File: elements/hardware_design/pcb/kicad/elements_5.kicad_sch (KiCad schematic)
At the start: 42 parts

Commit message: changed led/switch
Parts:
- removed SW1: (no value), symbol elements-eagle-import:LP4OA1PBCT
- added SW1: SW_MEC_5G_2LED, Supercell 1.3:C&K_D6R, symbol Switch:SW_MEC_5G_2LED
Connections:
- net GND: now also SW1.3 (K), SW1.4 (A)
- net SW_GATE: now also SW1.1
- net at R10.2: now also SW1.2
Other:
- moved on the sheet: R10

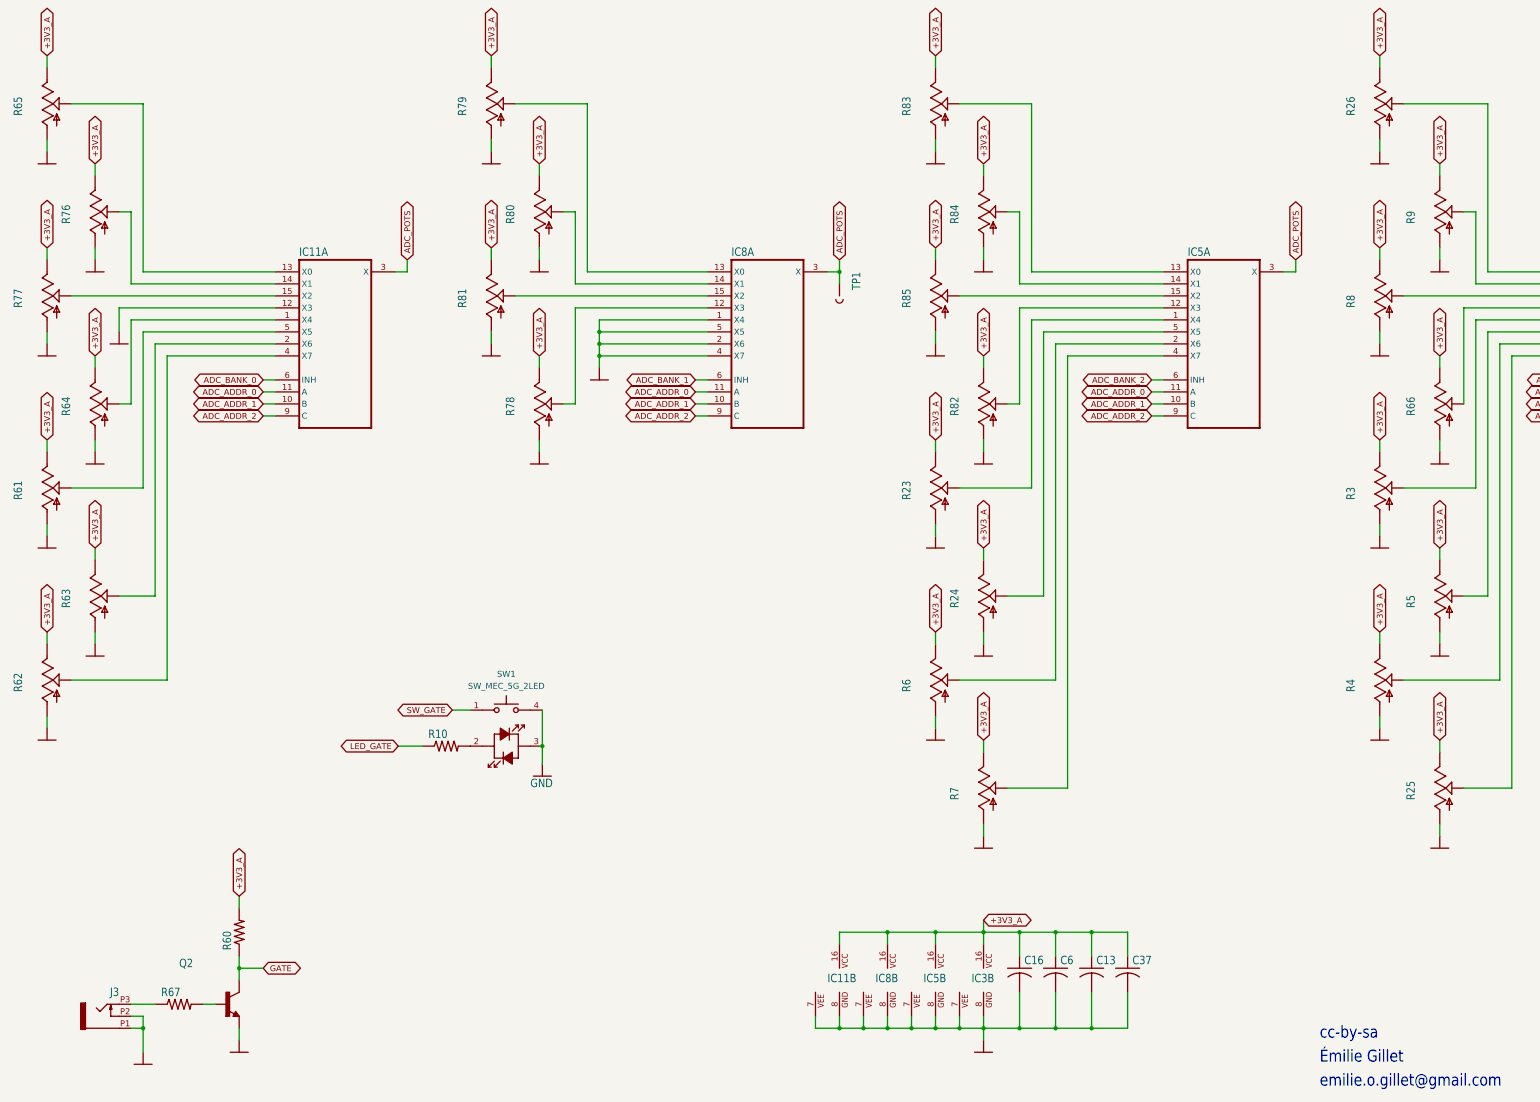
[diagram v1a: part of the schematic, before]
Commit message: swap wm8731 package (haven't drawn traces yet)
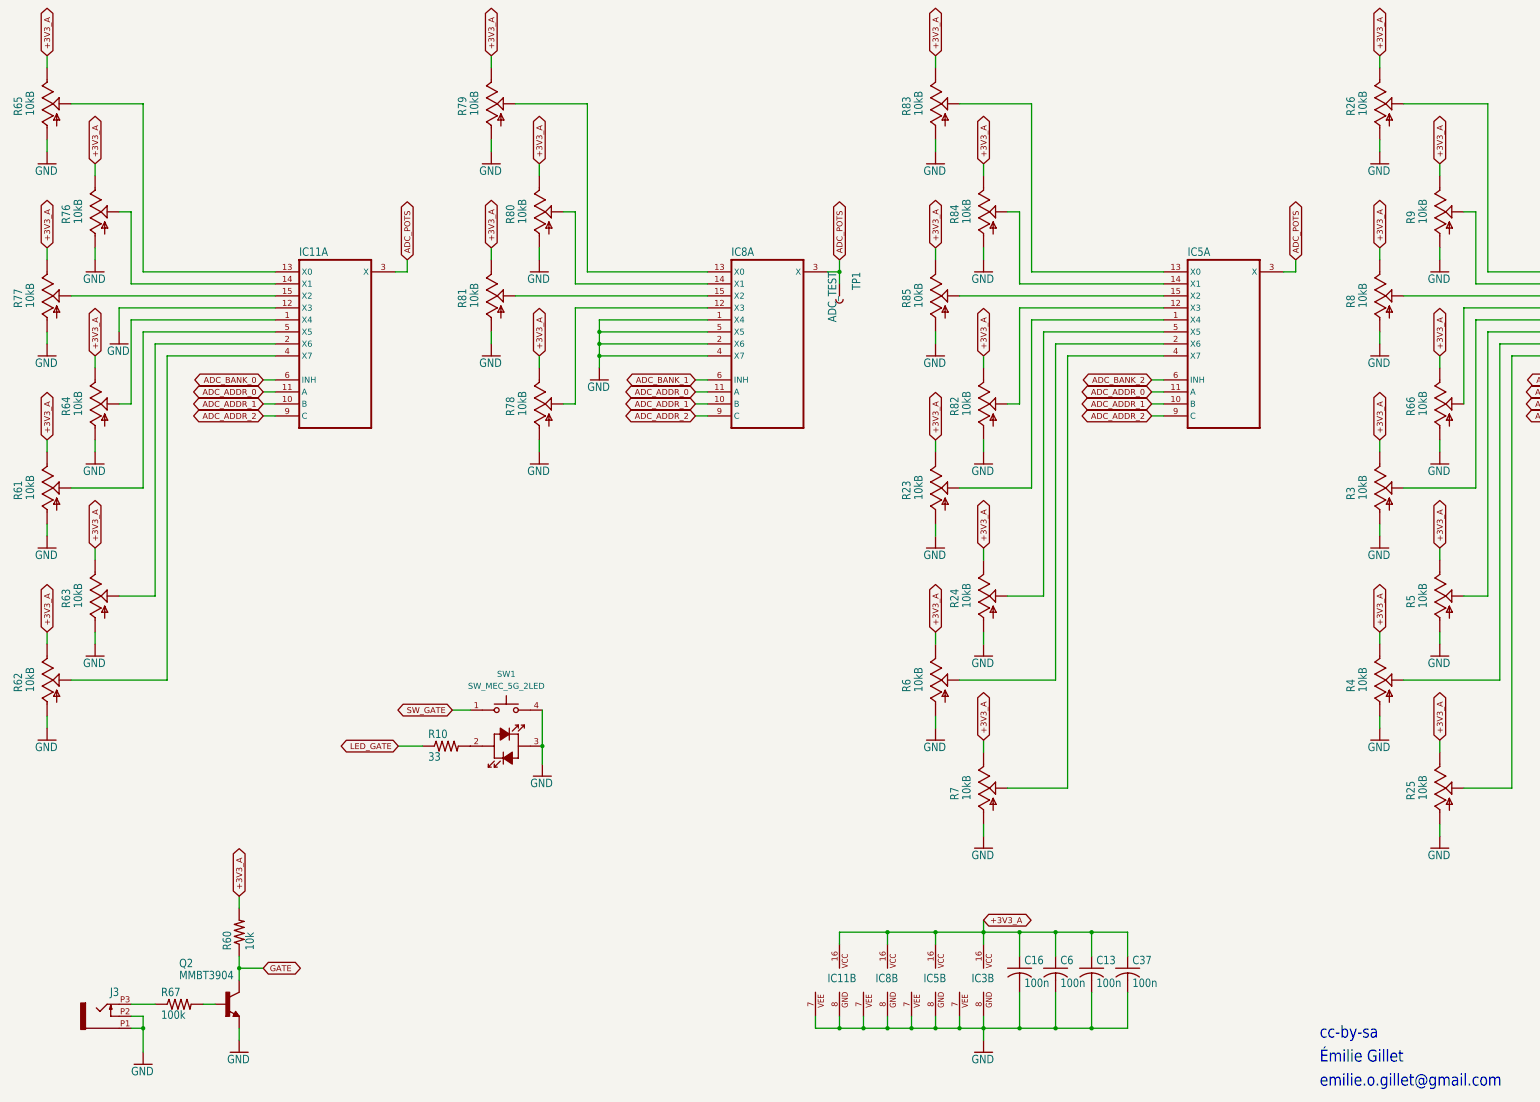
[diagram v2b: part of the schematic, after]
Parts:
- C13, C16, C37, C6: value (none) -> 100n; footprint (none) -> elements:C0603
- IC11, IC3, IC5, IC8: value (none) -> 4051PW; footprint (none) -> elements:TSSOP16
- J3: value (none) -> PJ301_THONKICONN6; footprint (none) -> elements:WQP_PJ_301M6
- Q2: value (none) -> MMBT3904; footprint (none) -> elements:SOT23-BEC
- R10: value (none) -> 33; footprint (none) -> elements:R0603
- R23, R24, R25, R26, R3, R4, R5, R6, R61, R62, R63, R64, R65, R66, R7, R8, R9: value (none) -> 10kB; footprint (none) -> elements:ALPS_POT_VERTICAL_PS
- R60: value (none) -> 10k; footprint (none) -> elements:R0603
- R67: value (none) -> 100k; footprint (none) -> elements:R0603
- R76, R77, R78, R79, R80, R81, R82, R83, R84, R85: value (none) -> 10kB; footprint (none) -> elements:ALPS_POT_VERTICAL
- TP1: value (none) -> ADC_TEST; footprint (none) -> elements:PAD.03X.03
